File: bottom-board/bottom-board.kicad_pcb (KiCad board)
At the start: 2 copper layers, 184 x 94 mm, 156 parts, among them P1 USB_B, P10 JACK_TRS_6PINS, P11 JACK_TRS_6PINS, P12 JACK_TRS_6PINS, P13 JACK_TRS_6PINS, P14 RJ45, P2 USB_A, P3 AudioJack3, P4 AS0A823-H4SB-7H, P5 BARREL_JACK, P6 AudioJack3, P7 AudioJack3, P8 HMI_DATA, P9 SERIAL_DEBUG, Q1 J110, Q12 2N7002, Q13 2N7002, Q2 J110, U1 TS2596, U10 RT9742MNGJ5, U11 6N137S, U12 ISL83491, U13 AP2120N-3.3, U2 LD1117S50TR_SOT223, U3 CODECODER-WM8731SEDS_V(SSOP28), U4 AT24CS08-STUM, U5 TS5A3159ADBVR

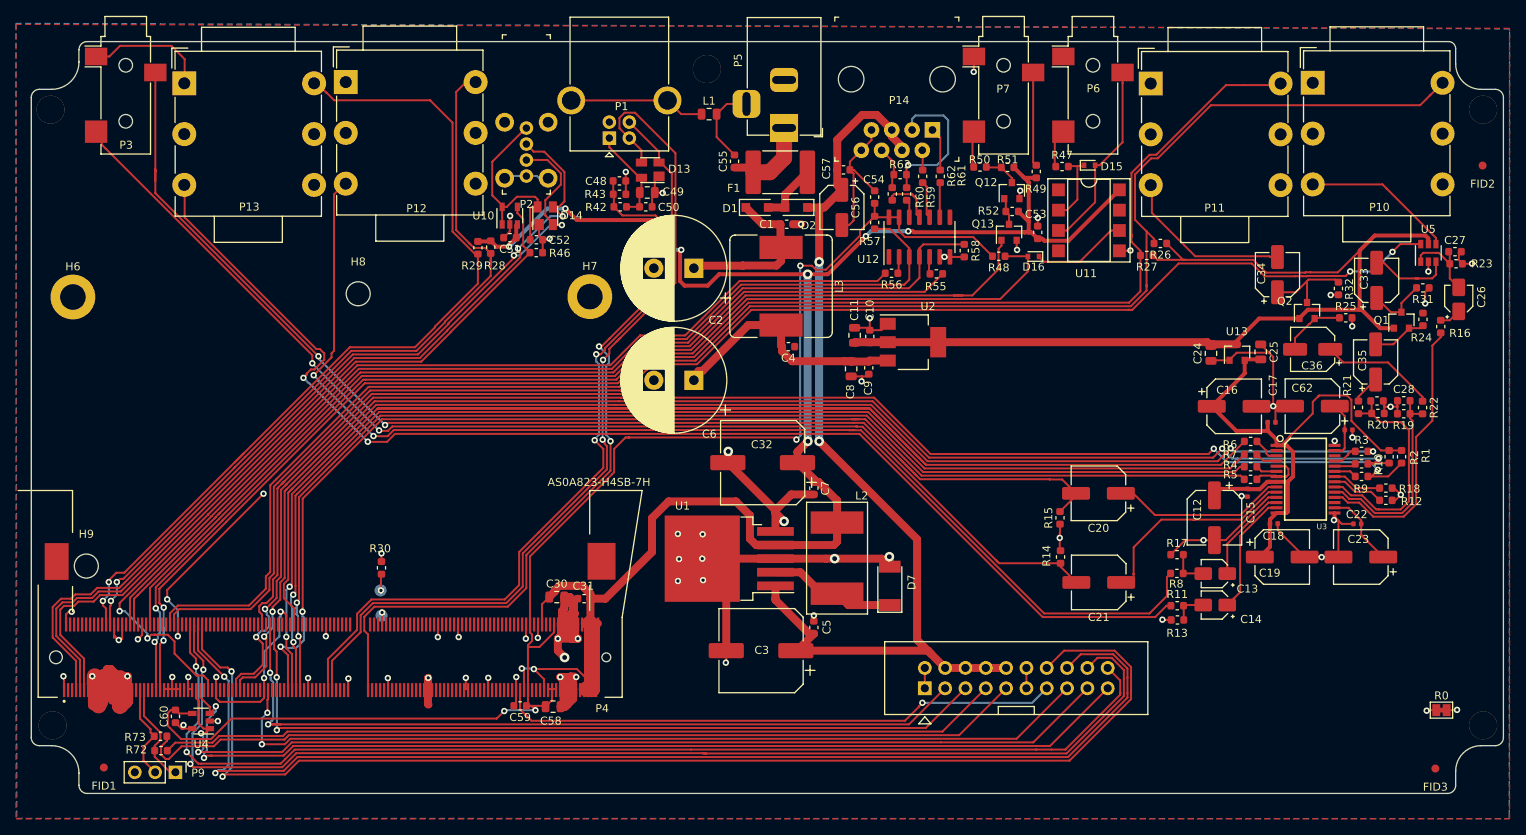
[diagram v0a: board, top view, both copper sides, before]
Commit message: reposistioned PSU filtering caps
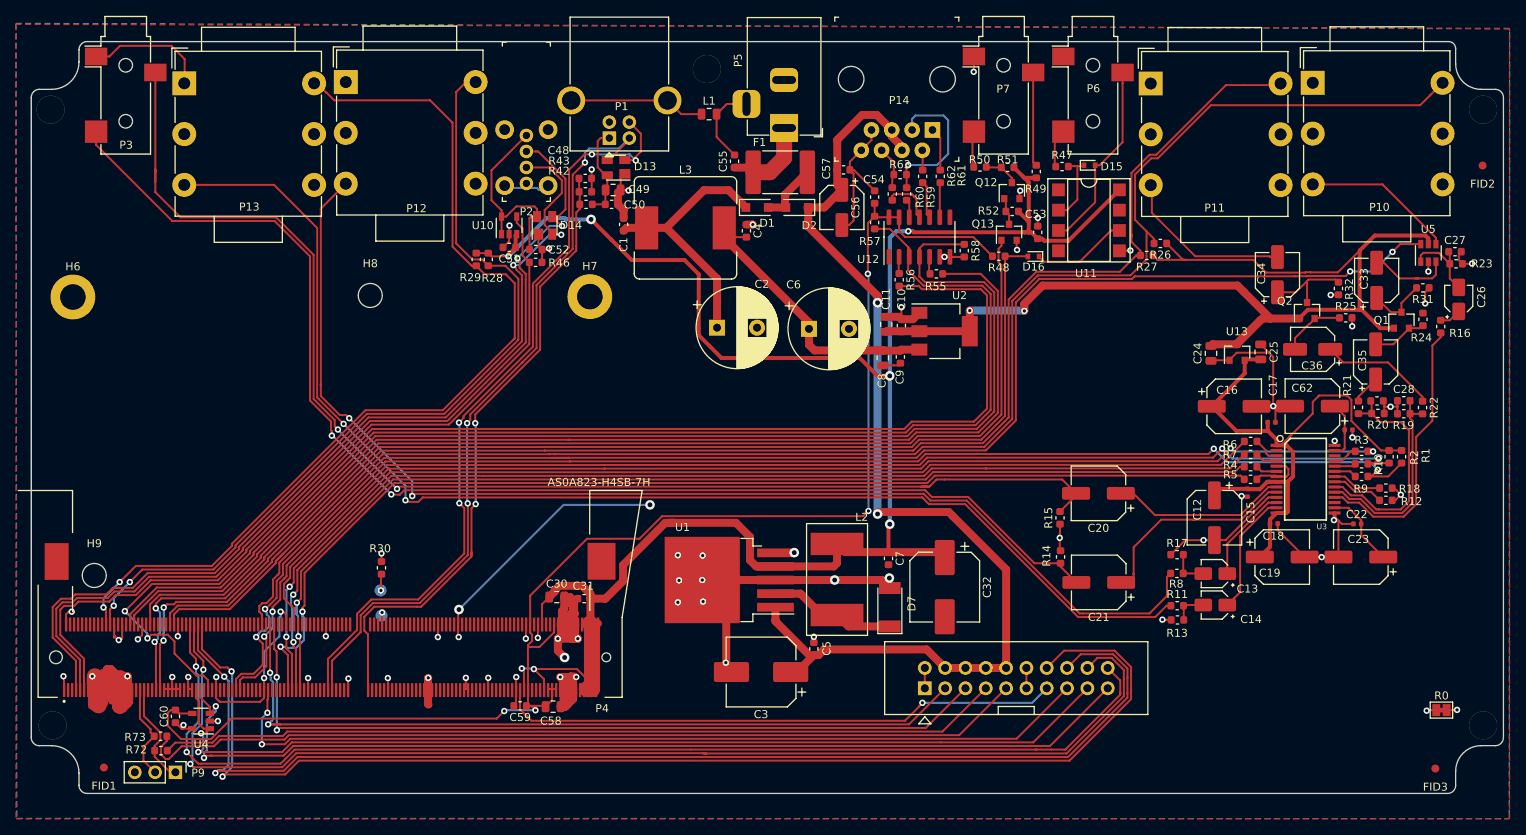
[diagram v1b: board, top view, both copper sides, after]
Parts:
- C2, C6: footprint Capacitor_THT:CP_Radial_D13.0mm_P5.00mm -> Capacitor_THT:CP_Radial_D10.0mm_P5.00mm
- C3, C32: footprint Capacitor_SMD:CP_Elec_10x7.9 -> Capacitor_SMD:CP_Elec_8x10.5
- moved C32 27.6 mm to (177.6, 109.0), turned to 270 degrees
- moved C1 20.4 mm to (137.4, 63.6), turned to 90 degrees
- moved C6 15.8 mm to (160.6, 76.7), turned to 0 degrees
- moved C4 15.4 mm to (152.8, 64.4), turned to 90 degrees
- moved L3 14.0 mm to (145.2, 64.0), turned to 0 degrees
- moved C7 12.8 mm to (170.5, 105.4)
- moved C2 7.98 mm to (149.1, 76.5), turned to 0 degrees
- moved R43 4.28 mm to (132.6, 59.5)
- moved C48 4.28 mm to (132.6, 57.9)
- moved C49 4.28 mm to (136.1, 59.3)
- moved C50 4.28 mm to (135.9, 61.1)
- moved D13 4.28 mm to (136.5, 56.5)
- moved R42 4.28 mm to (132.7, 61.1)
- moved C11 4.18 mm to (170.2, 76.1)
- moved C9 4.18 mm to (172.0, 80.2)
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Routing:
- net CODEC_I2S_BCLK: track 224.1 -> 141.2 mm
- net +12V: track 212.9 -> 134.7 mm
- net CHAIN_UART_RX: track 131.4 -> 161.4 mm
- net CHAIN_UART_RE: track 126.4 -> 154.9 mm
- net CHAIN_UART_DE: track 127.5 -> 153.8 mm
- net CHAIN_UART_TX: track 119.8 -> 141.9 mm
- net +5VA: track 127.9 -> 146.3 mm, vias 0 -> 2
- net USB_DEV_DM: track 111.6 -> 94.1 mm, vias 2 -> 3
- net USB_DEV_DET: track 97.6 -> 80.1 mm
- net CODEC_I2S_LRCK: track 152.7 -> 140.4 mm
- net HEADPHONE_RIGHT: track 148.5 -> 160.2 mm
- net CODEC_I2C_SDA: track 182.2 -> 170.6 mm
- net CODEC_I2C_SCL: track 178.3 -> 166.7 mm
- net CODEC_I2S_MCLK: track 162.0 -> 150.4 mm
- net +5V: track 260.6 -> 272.1 mm, vias 10 -> 7
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
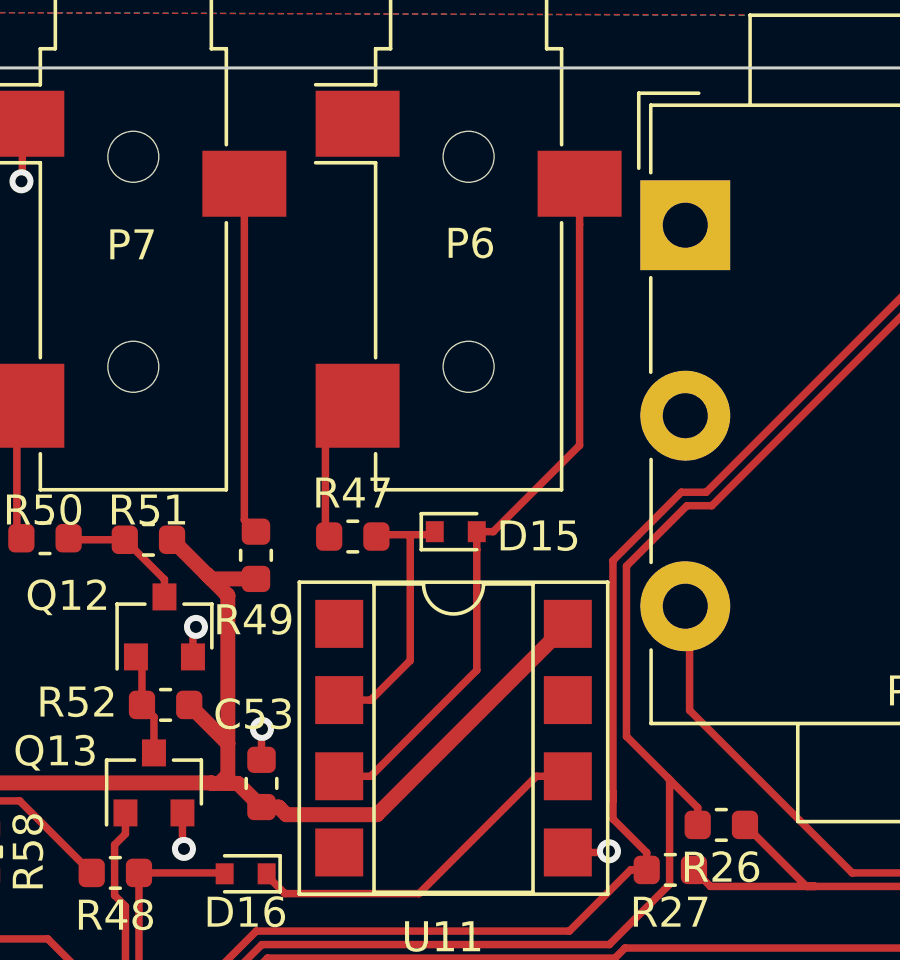
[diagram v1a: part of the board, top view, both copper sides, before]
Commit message: change on MIDI input to TRS type A standart + cleanup
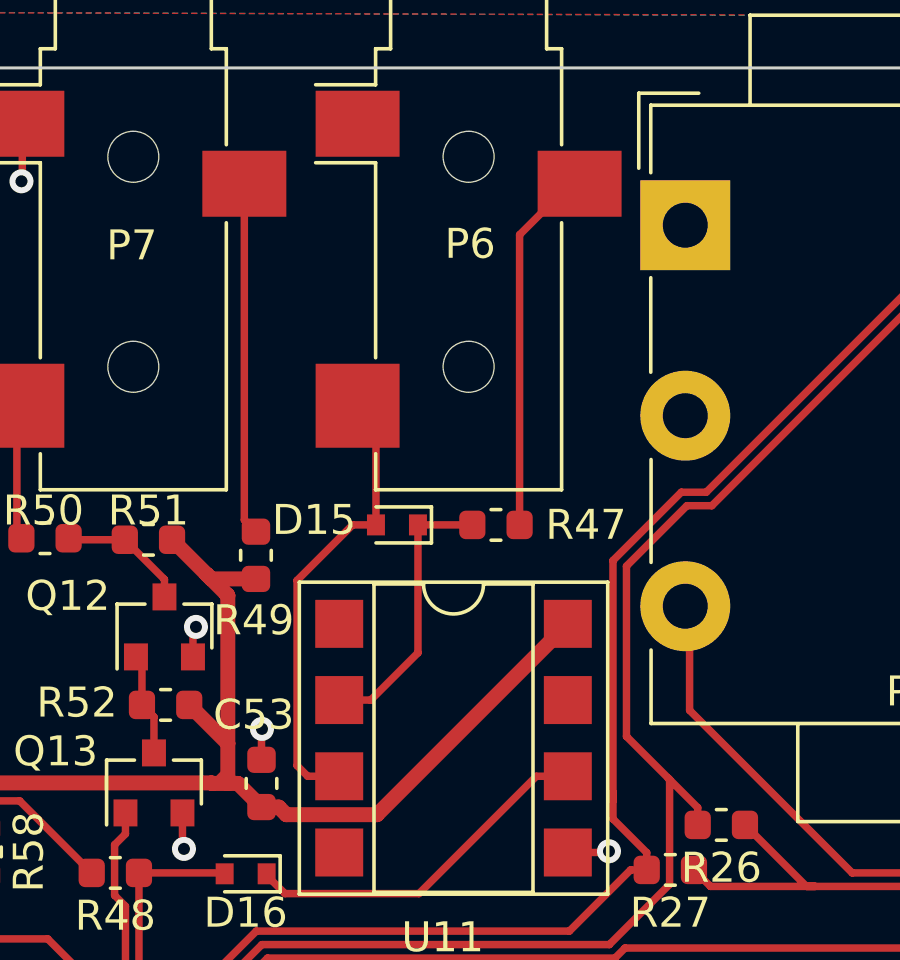
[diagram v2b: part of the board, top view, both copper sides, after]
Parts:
- moved R47 4.79 mm to (197.0, 56.0), turned to 180 degrees
- moved D15 1.97 mm to (193.7, 56.0), turned to 180 degrees
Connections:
- P6 pad R: Net-(D15-Pad2) -> Net-(P6-PadR)
- P6 pad T: Net-(P6-PadT) -> Net-(D15-Pad2)
- R47 pad 1: Net-(P6-PadT) -> Net-(P6-PadR)
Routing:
- net Net-(P6-PadR): track 0.00 -> 12.4 mm
- net Net-(D15-Pad2): track 24.0 -> 15.3 mm
- net Net-(P6-PadT): track 4.74 -> 0.00 mm
